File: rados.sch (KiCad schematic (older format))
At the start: 1 part

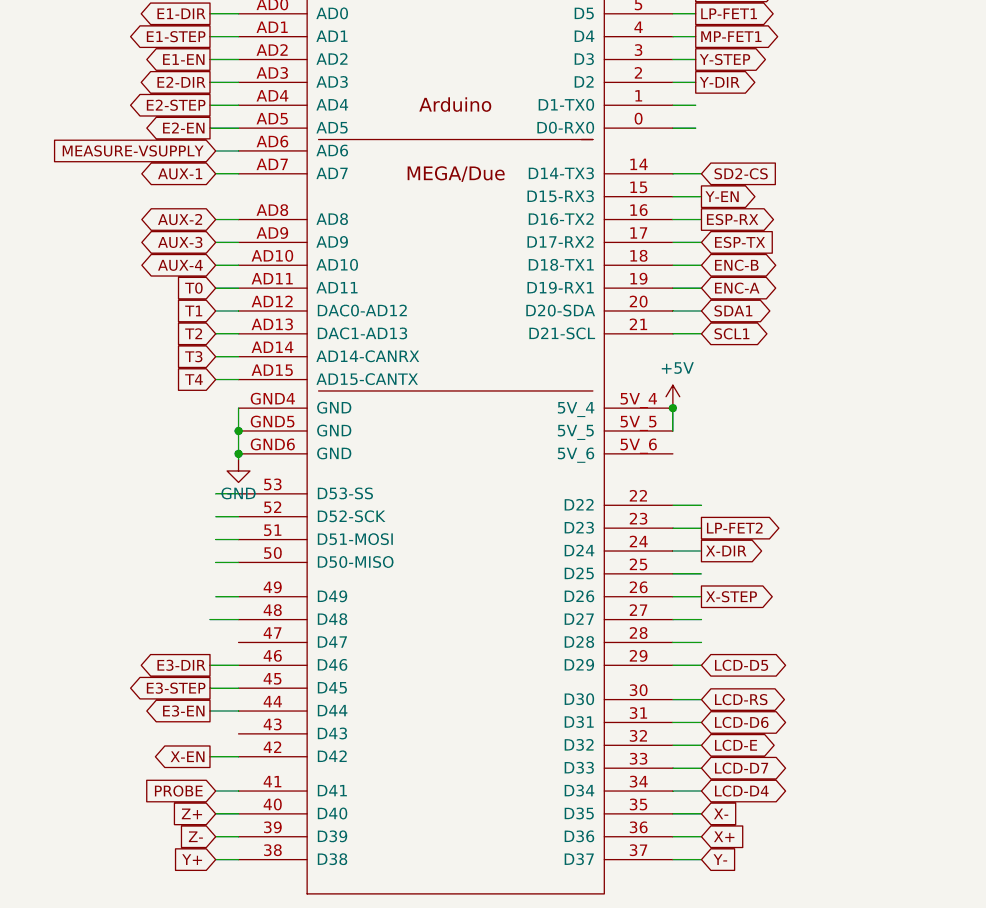
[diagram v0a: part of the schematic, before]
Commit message: fix analog and wifi
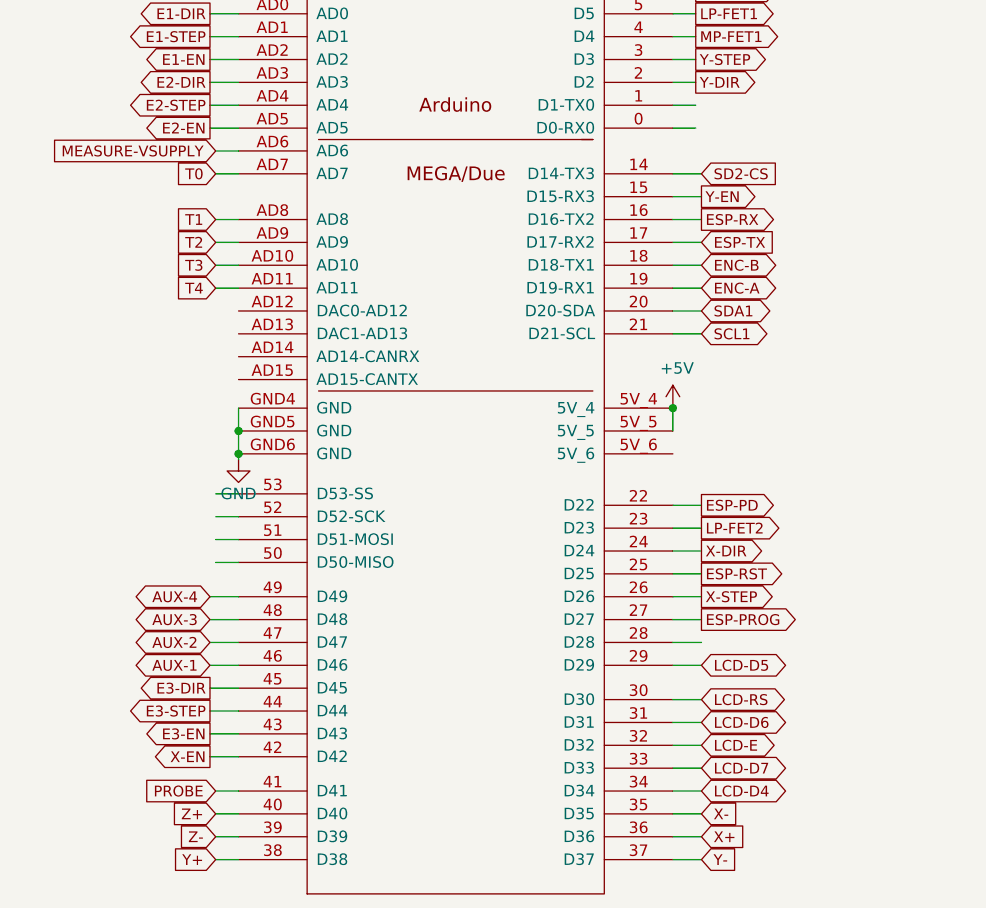
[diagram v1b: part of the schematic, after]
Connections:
- net labels added: ESP-PD, ESP-PROG, ESP-RST
- wire segments 80 -> 78
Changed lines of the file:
@@
 Text GLabel 5125 4100 2    47   BiDi ~ 0
 ENC-A
+Text GLabel 2975 6050 0    47   Output ~ 0
+E3-EN
 Text GLabel 2975 5950 0    47   Output ~ 0
-E3-EN
+E3-STEP
 Text GLabel 2975 5850 0    47   Output ~ 0
-E3-STEP
-Text GLabel 2975 5750 0    47   Output ~ 0
 E3-DIR
 $Comp
@@
 Text GLabel 2975 2900 0    47   Output ~ 0
 E1-DIR
+Text GLabel 3000 3600 0    47   Input ~ 0
+T0
+Text GLabel 3000 3800 0    47   Input ~ 0
+T1
+Text GLabel 3000 3900 0    47   Input ~ 0
+T2
+Text GLabel 3000 4000 0    47   Input ~ 0
+T3
 Text GLabel 3000 4100 0    47   Input ~ 0
-T0
-Text GLabel 3000 4200 0    47   Input ~ 0
-T1
-Text GLabel 3000 4300 0    47   Input ~ 0
-T2
-Text GLabel 3000 4400 0    47   Input ~ 0
-T3
-Text GLabel 3000 4500 0    47   Input ~ 0
 T4
 Text GLabel 5100 2000 2    47   Output ~ 0
@@
 Text GLabel 3000 6300 0    47   Input ~ 0
 PROBE
-Text GLabel 3000 3600 0    47   BiDi ~ 0
+Text GLabel 2975 5750 0    47   BiDi ~ 0
 AUX-1
-Text GLabel 3000 3800 0    47   BiDi ~ 0
+Text GLabel 2975 5650 0    47   BiDi ~ 0
 AUX-2
-Text GLabel 3000 3900 0    47   BiDi ~ 0
+Text GLabel 2975 5550 0    47   BiDi ~ 0
 AUX-3
-Text GLabel 3000 4000 0    47   BiDi ~ 0
+Text GLabel 2975 5450 0    47   BiDi ~ 0
 AUX-4
 Text GLabel 5125 3800 2    47   Output ~ 0
@@
 	5125 6200 5000 6200
 Wire Wire Line
+	3000 5300 3100 5300
+Wire Wire Line
+	3100 5100 3000 5100
+Wire Wire Line
+	3000 5000 3100 5000
+Wire Wire Line
+	3100 5200 3000 5200
+Wire Wire Line
+	3100 4625 3100 4850
+Wire Wire Line
+	2975 3400 3100 3400
+Wire Wire Line
+	3100 5450 2975 5450
+Wire Wire Line
 	2975 5550 3100 5550
 Wire Wire Line
-	3000 5300 3100 5300
-Wire Wire Line
-	3100 5100 3000 5100
-Wire Wire Line
-	3000 5000 3100 5000
-Wire Wire Line
-	3100 5200 3000 5200
-Wire Wire Line
-	3000 5450 3100 5450
-Wire Wire Line
-	3100 4625 3100 4850
-Wire Wire Line
-	2975 3400 3100 3400
+	2975 5650 3100 5650
+Wire Wire Line
+	3100 5750 2975 5750
+Wire Wire Line
+	3000 3500 3100 3500
+Wire Wire Line
+	3000 2700 3100 2700
+Wire Wire Line
+	3000 2200 3100 2200
+Wire Wire Line
+	3000 4100 3100 4100
 Wire Wire Line
 	3100 4000 3000 4000
@@
 	3000 3900 3100 3900
 Wire Wire Line
-	3000 3800 3100 3800
-Wire Wire Line
-	3100 3600 3000 3600
-Wire Wire Line
-	3000 3500 3100 3500
-Wire Wire Line
-	3000 2700 3100 2700
-Wire Wire Line
-	3000 2200 3100 2200
-Wire Wire Line
-	3000 4500 3100 4500
-Wire Wire Line
-	3100 4400 3000 4400
-Wire Wire Line
-	3000 4300 3100 4300
-Wire Wire Line
-	3100 4200 3000 4200
-Wire Wire Line
-	3000 4100 3100 4100
+	3100 3800 3000 3800
+Wire Wire Line
+	3000 3600 3100 3600
 Wire Wire Line
 	3000 6300 3100 6300
@@
 	5125 5750 5000 5750
 Wire Wire Line
-	2975 5750 3100 5750
+	2975 5850 3100 5850
+Wire Wire Line
+	2975 6050 3100 6050
 Wire Wire Line
 	2975 5950 3100 5950
-Wire Wire Line
-	2975 5850 3100 5850
 Wire Wire Line
 	5100 2800 5000 2800
@@
 	1    0    0    -1
 $EndComp
+Text GLabel 5125 5350 2    47   Output ~ 0
+ESP-RST
+Text GLabel 5125 5550 2    47   Output ~ 0
+ESP-PROG
+Text GLabel 5125 5050 2    47   Output ~ 0
+ESP-PD
 $EndSCHEMATC
